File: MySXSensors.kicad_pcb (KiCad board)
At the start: 2 copper layers, 27.7 x 44 mm, 13 parts, among them J1 LD2410B, J2 UART, J3 I2C, J5 PinSocket_1x01_P2.54mm_Vertic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, J6 PinSocket_1x01_P2.54mm_Vertic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, U1 BME280, U2 BH1750FVI-TR

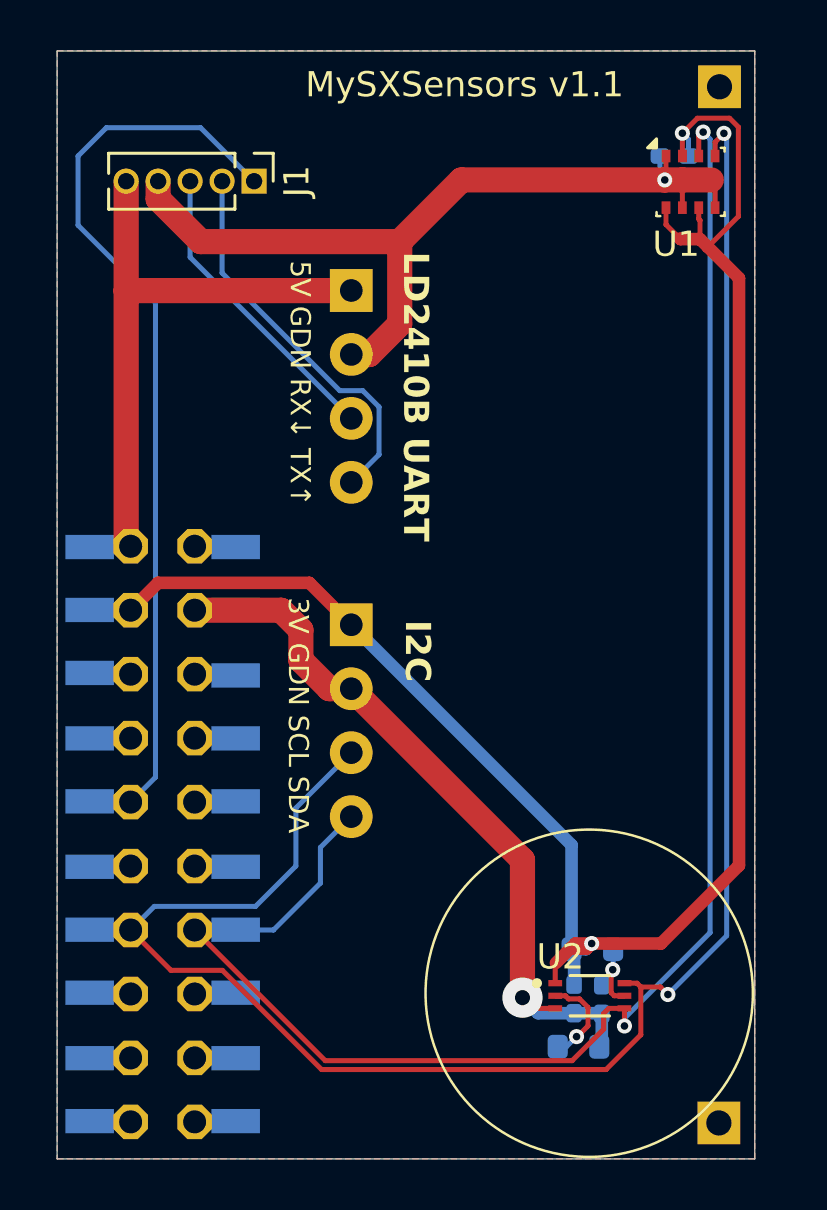
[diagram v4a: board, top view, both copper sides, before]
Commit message: change motion signal assignment to D4_INT
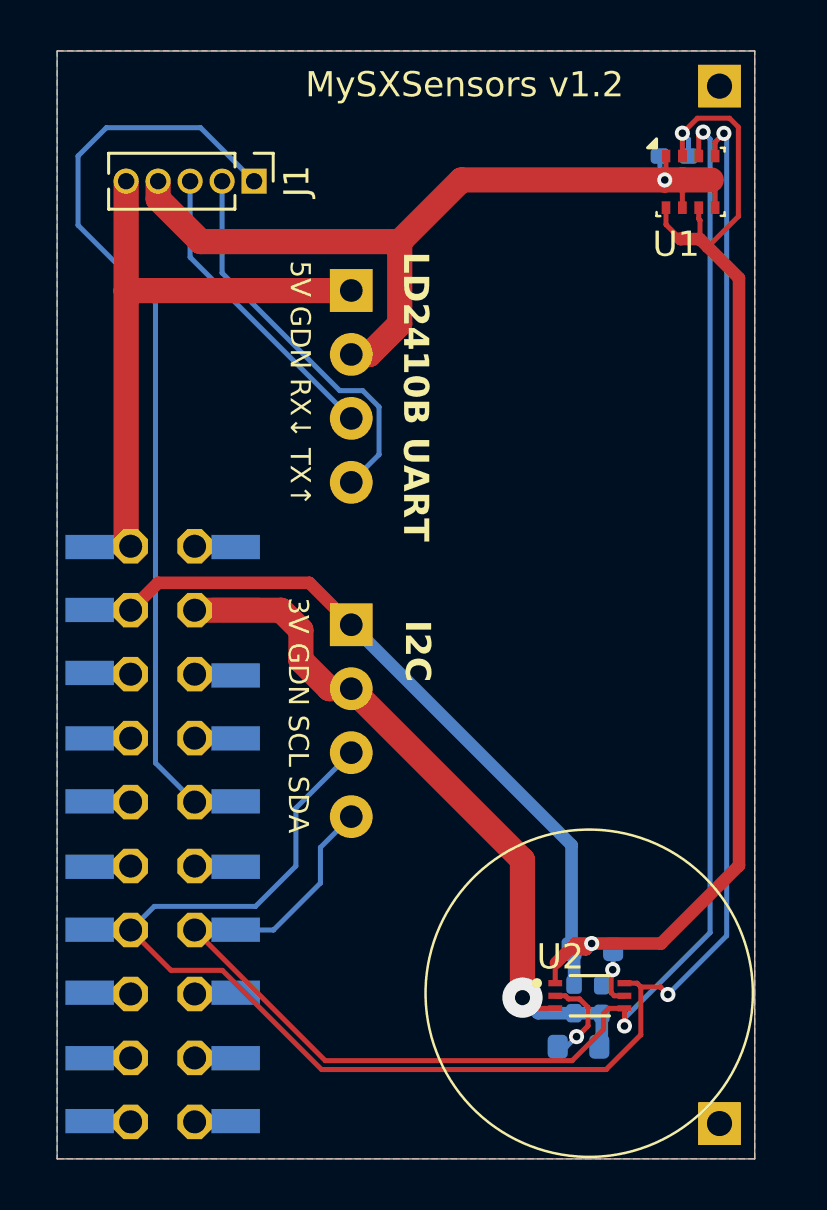
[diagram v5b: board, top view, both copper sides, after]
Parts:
- removed J5, J6: PinSocket_1x01_P2.54mm_Vertical, Connector_PinSocket_2.54mm:PinSocket_1x01_P2.54mm_Vertical
- added REF**: PinSocket_1x01_P2.54mm_Vertical, Connector_PinSocket_2.54mm:PinSocket_1x01_P2.54mm_Vertical, B.Cu at (161.6, 122.8)
- added REF**: PinSocket_1x01_P2.54mm_Vertical, Connector_PinSocket_2.54mm:PinSocket_1x01_P2.54mm_Vertical, B.Cu at (161.6, 81.7)
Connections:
- J1 pad 1: D3_INT -> D4_INT
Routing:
- net D4_INT: track 0.00 -> 35.9 mm
- net D3_INT: track 35.7 -> 0.00 mm
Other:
- board text added: "MySXSensors v1.2"
- board text removed: "MySXSensors v1.1"

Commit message: add lens footprint
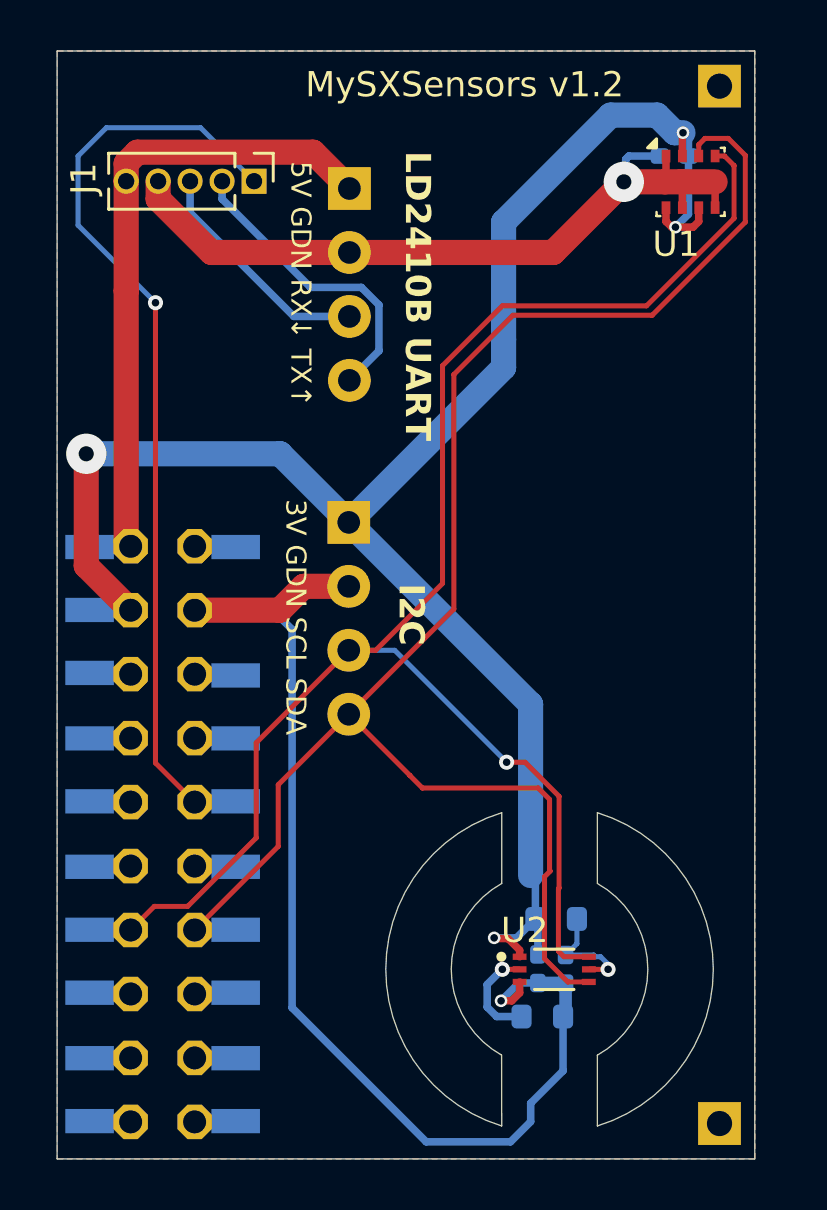
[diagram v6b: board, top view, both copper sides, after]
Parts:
- added L1: Lens, MySXSensors:Lens, F.Cu at (154.8, 116.7)
- moved J3 4.07 mm to (146.9, 96.4)
- moved J2 4.05 mm to (146.9, 83.2)
- moved C2 1.87 mm to (154.4, 116.7)
- moved C3 1.87 mm to (155.5, 116.7)
- moved R1 1.87 mm to (154.6, 118.6)
- moved R2 1.87 mm to (155.1, 114.7)
- moved U2 1.76 mm to (155.0, 116.7)
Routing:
- net GND: track 63.9 -> 76.7 mm
- net D7_SCL: track 76.2 -> 64.2 mm, vias 2 -> 1
- net VCCIO: track 78.2 -> 73.4 mm, vias 2 -> 4
- net D8_SDA: track 68.1 -> 63.7 mm, vias 2 -> 0
- net Net-(J1-Pin_2): track 15.5 -> 12.2 mm
- net Net-(J1-Pin_3): track 12.1 -> 9.28 mm
- net VRAW: track 23.6 -> 24.9 mm
- net Net-(U2-DVI): track 3.13 -> 4.42 mm
- net D4_INT: vias 0 -> 1
